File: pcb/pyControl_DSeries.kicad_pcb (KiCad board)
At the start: 2 copper layers, 90.2 x 66.5 mm, 14 parts, among them J1 Barrel_Jack, J2 RJ45-12PORT, U1 PyBoard-D-Series, U2 MC7805_DPAK, U3 TBD62083APG, U4 TBD62083APG, U5 TBD62083APG

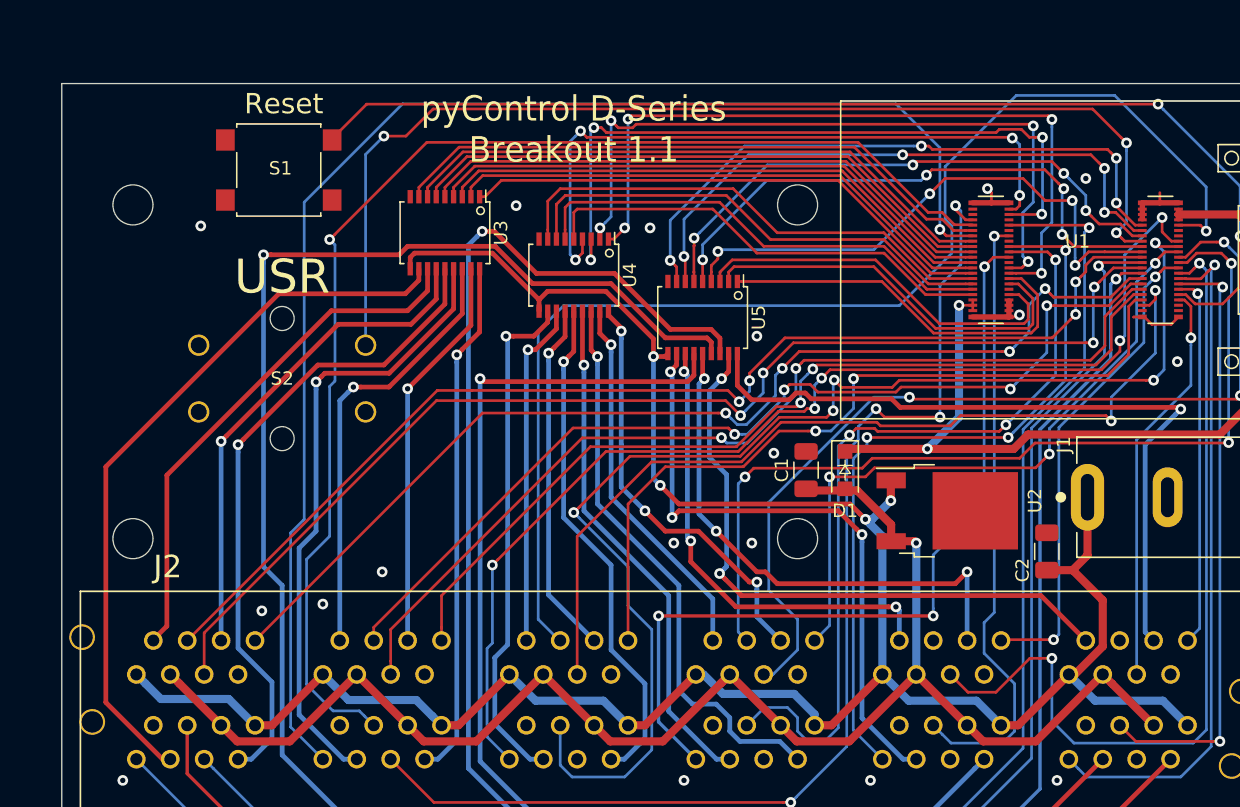
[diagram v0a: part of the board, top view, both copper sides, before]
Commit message: Revised PCB to v1.2 Switched from linear regulator to DC-DC converter. 1µF capacitors are now 10µF. Added TAPR link to silkscreen and schematic.
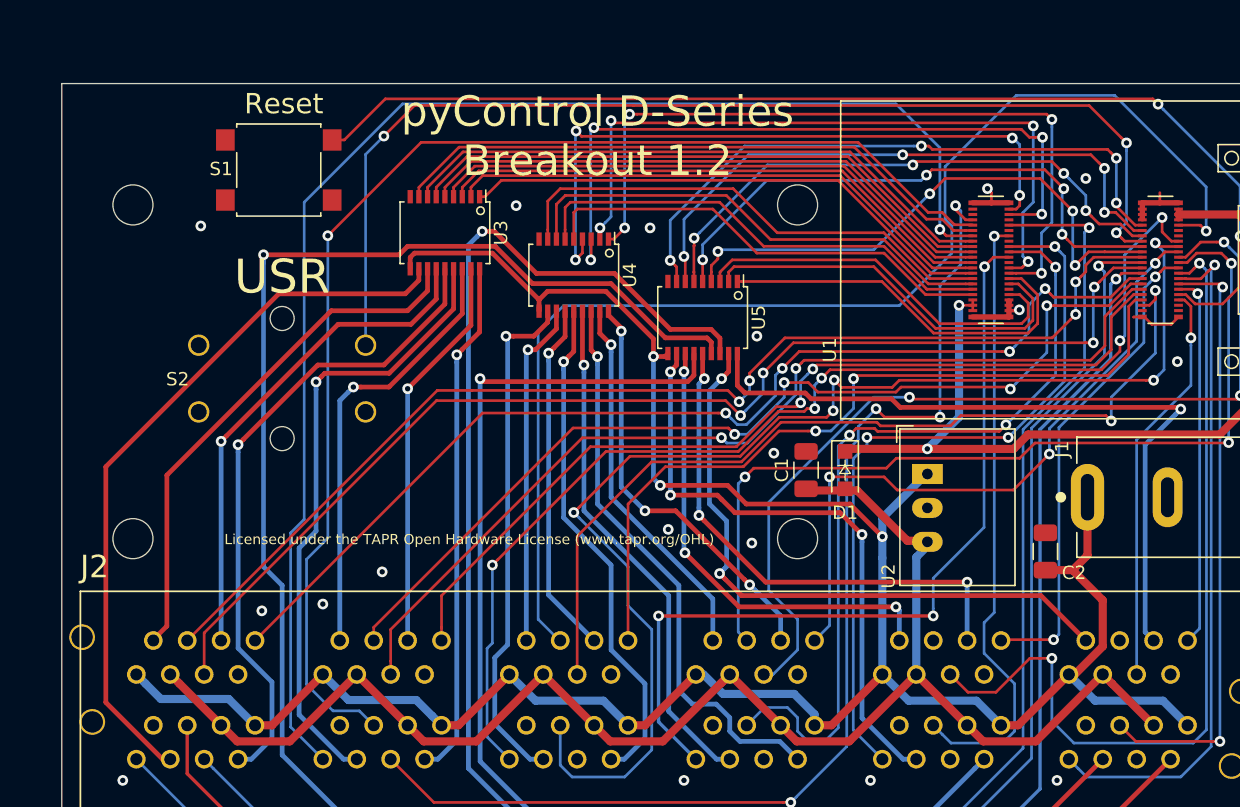
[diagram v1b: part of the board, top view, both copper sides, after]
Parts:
- C1, C2: value 1µF -> 10µF
- D1: footprint Andy_footprints:D_SOD-123F -> asl_footprints:D_SOD-123F
- DRA1, DRA2: footprint Andy_footprints:DIN_Clip -> asl_footprints:DIN_Clip
- J1: footprint Andy_footprints:DC_Jack -> asl_footprints:DC_Jack
- J2: footprint Andy_footprints:RJ45_12Port -> asl_footprints:RJ45_12Port
- S1: footprint Andy_footprints:6mm_tactile_smd -> asl_footprints:6mm_tactile_smd
- S2: footprint Andy_footprints:12mm_tactile_SPST -> asl_footprints:12mm_tactile_SPST
- U1: footprint Andy_footprints:PyBoard_D-Series -> asl_footprints:PyBoard_D-Series
- U2: value MC7805_DPAK -> R-78E5.0-1.0; footprint Andy_footprints:TO-252-2 -> asl_footprints:Converter_DCDC_RECOM_R-78E-0.5_THT
- U3, U4, U5: footprint Andy_footprints:SSOP-18_4.4x6.5mm_P0.65mm -> asl_footprints:SSOP-18_4.4x6.5mm_P0.65mm
- moved U2 3.13 mm to (116.9, 115.1), turned to 270 degrees
- moved C2 0.11 mm to (125.8, 120.9)
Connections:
- J2 pad B3-5: Net-(J2-PadB3-5) -> (no net)
- J2 pad B4-5: Net-(J2-PadB4-5) -> (no net)
- J2 pad B5-5: Net-(J2-PadB5-5) -> (no net)
- J2 pad B6-5: Net-(J2-PadB6-5) -> (no net)
- J2 pad S1: Net-(J2-PadS1) -> (no net)
- J2 pad S2: Net-(J2-PadS2) -> (no net)
- J2 pad S3: Net-(J2-PadS3) -> (no net)
- J2 pad S4: Net-(J2-PadS4) -> (no net)
- J2 pad S5: Net-(J2-PadS5) -> (no net)
- J2 pad S6: Net-(J2-PadS6) -> (no net)
- J2 pad T5-5: Net-(J2-PadT5-5) -> (no net)
- J2 pad T6-5: Net-(J2-PadT6-5) -> (no net)
- S1 pad 4: Net-(S1-Pad4) -> (no net)
- S2 pad 1: Net-(S2-Pad1) -> (no net)
- S2 pad 4: Net-(S2-Pad4) -> (no net)
- U1 pad 13: Net-(U1-Pad13) -> (no net)
- U1 pad 2: Net-(U1-Pad2) -> (no net)
- U1 pad 21: Net-(U1-Pad21) -> (no net)
- U1 pad 31: Net-(U1-Pad31) -> (no net)
- U1 pad 4: Net-(U1-Pad4) -> (no net)
- U1 pad 41: Net-(U1-Pad41) -> (no net)
- U1 pad 42: Net-(U1-Pad42) -> (no net)
- U1 pad 44: Net-(U1-Pad44) -> (no net)
- U1 pad 5: Net-(U1-Pad5) -> (no net)
- U1 pad 70: Net-(U1-Pad70) -> (no net)
- U1 pad 9: Net-(U1-Pad9) -> (no net)
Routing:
- net /12VDC: track 183.6 -> 186.2 mm, vias 4 -> 3
- net /B5_PA: track 46.8 -> 45.4 mm
- net /T5_PA: track 40.0 -> 38.9 mm
- net /5VDC: track 117.2 -> 118.3 mm, vias 1 -> 0
- net /T4_DA: track 49.6 -> 50.5 mm
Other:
- board text added: "Licensed under the TAPR Open Hardware License (www.tapr.org/OHL)"
- board text added: "pyControl D-Series Breakout 1.2"
- board text removed: "pyControl D-Series Breakout 1.1"

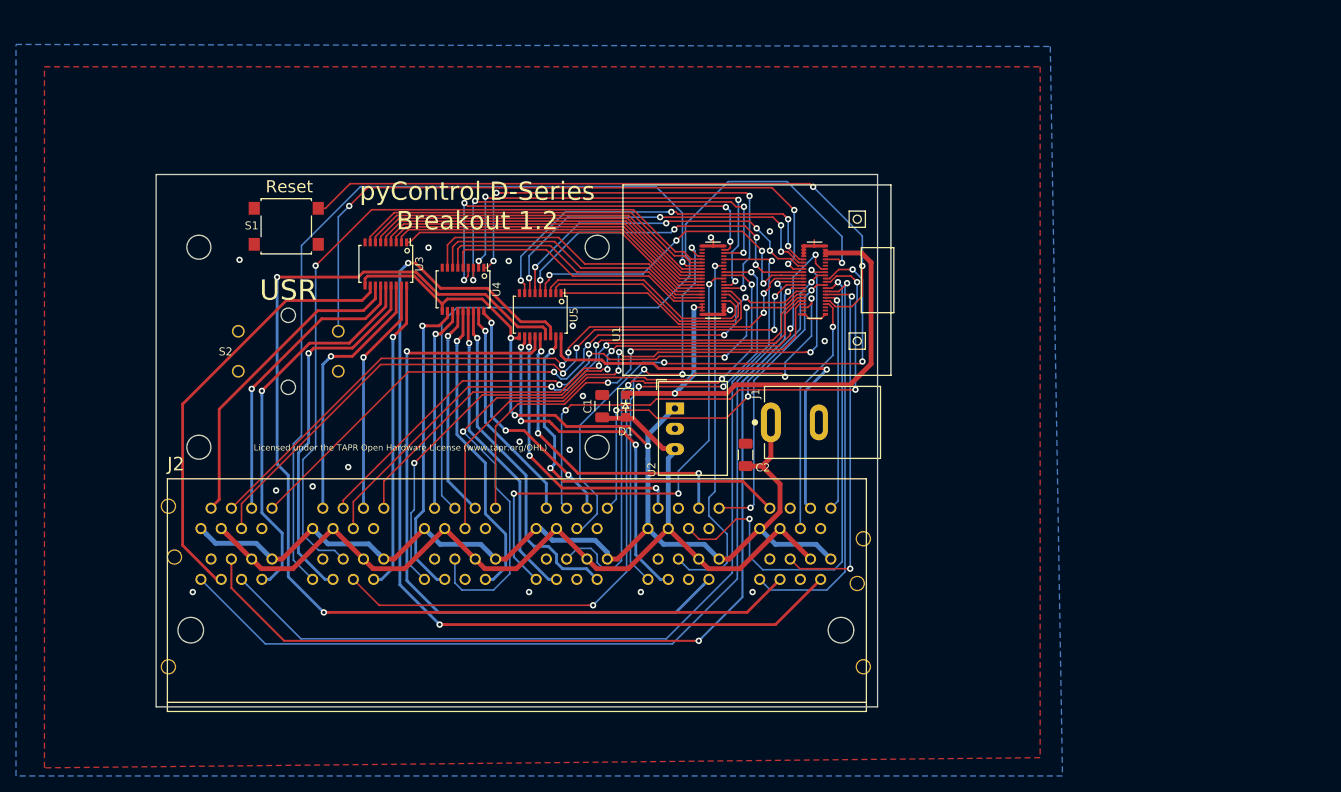
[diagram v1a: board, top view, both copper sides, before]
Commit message: pcb version 1.3. W1 cannot be used as DIO, so now B4_COMA is connected to pin9 (W9). W69 cannot be used as DIO, so now B5_COMB is connected to pin5 (W5). Added microusb connector so that you can permanently plug into breakout board and talk to the pyboard via the Hirose connector. This enables usb communication with the pyboard while still allowing one to easily swap out pyboards if necessary. changed user switch to SMD part Shifted components around.
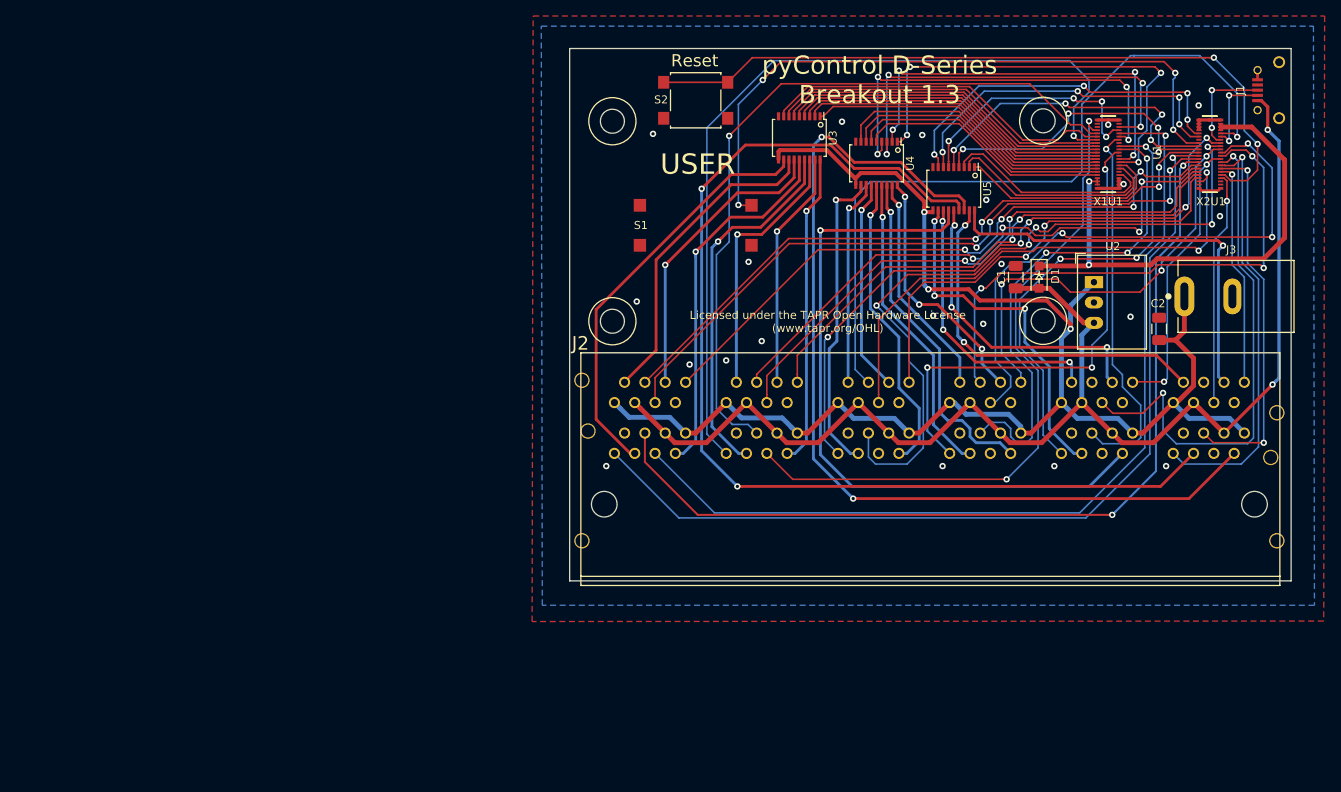
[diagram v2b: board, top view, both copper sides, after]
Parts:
- added J1: USB_micro_horz_socket_reinforced, asl_footprints:microUSB_horizontal_socket, F.Cu at (191.2, 75.3)
- added X1U1: Hirose_40_pin_connector, asl_footprints:Hirose_40_pin, F.Cu at (171.1, 83.3)
- added X2U1: Hirose_40_pin_connector, asl_footprints:Hirose_40_pin, F.Cu at (183.8, 83.3)
- S1: value B3FS-1010P -> TL3300; footprint asl_footprints:6mm_tactile_smd -> asl_footprints:12mm_tactile_smd
- S2: value B3F-4000 -> B3FS-1010P; footprint asl_footprints:12mm_tactile_SPST -> asl_footprints:6mm_tactile_smd
- moved S2 59.8 mm to (119.5, 76.6)
- moved DRA2 57.9 mm to (162.9, 91.6)
- moved U2 54.7 mm to (169.3, 99.3)
- moved C1 54.1 mm to (159.5, 98.7)
- moved D1 54.1 mm to (162.4, 98.7)
- moved J2 54.0 mm to (148.8, 122.7)
- moved J3 54.0 mm to (180.6, 101.1)
- moved U3 54.0 mm to (132.5, 81.3)
- moved U4 54.0 mm to (142.1, 84.5)
- moved U5 54.0 mm to (151.8, 87.6)
- moved DRA1 54.0 mm to (109.1, 91.7)
- moved C2 54.0 mm to (177.4, 105.2)
- moved U1 51.9 mm to (177.4, 83.3)
- moved S1 51.2 mm to (119.5, 92.2)
- renumbered J1 to J3
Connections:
- S1 pad 3: /RST -> /USR
- S2 pad 1: (no net) -> /GND
- S2 pad 3: /USR -> /RST
- S2 pad 4: (no net) -> /RST
- U1 pad 1: /B4_COMA -> (no net)
- U1 pad 5: (no net) -> /B5_COMB
- U1 pad 69: /B5_COMB -> (no net)
- U1 pad 70: (no net) -> Net-(J1-PadP3)
- U1 pad 72: (no net) -> Net-(J1-PadP2)
- U1 pad 9: (no net) -> /B4_COMA
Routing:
- net /5VDC: track 118.3 -> 165.0 mm, vias 0 -> 2
- net Net-(J1-PadP3): track 0.00 -> 12.7 mm, vias 0 -> 2
- net /B5_COMB: track 42.2 -> 31.4 mm
- net Net-(J1-PadP2): track 0.00 -> 10.6 mm, vias 0 -> 2
- net /RST: track 84.9 -> 91.5 mm
- net /B6_PA: track 140.7 -> 136.1 mm
- net /B3_DA: track 84.0 -> 79.5 mm
- net /T4_DA: track 50.5 -> 54.0 mm
- net /B6_COMA: track 41.9 -> 38.4 mm
- net /B3_DB: track 93.3 -> 90.1 mm
- net /T6_PA: track 55.0 -> 51.9 mm
- net /T1_DB: track 88.9 -> 85.9 mm
- net /B3_COMB: track 34.6 -> 31.7 mm
- net /T1_DC: track 86.7 -> 83.7 mm
- net /T3_COMA: track 35.8 -> 32.9 mm
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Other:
- board text added: "USER"
- board text added: "pyControl D-Series Breakout 1.3"
- board text removed: "USR"
- board text removed: "pyControl D-Series Breakout 1.2"

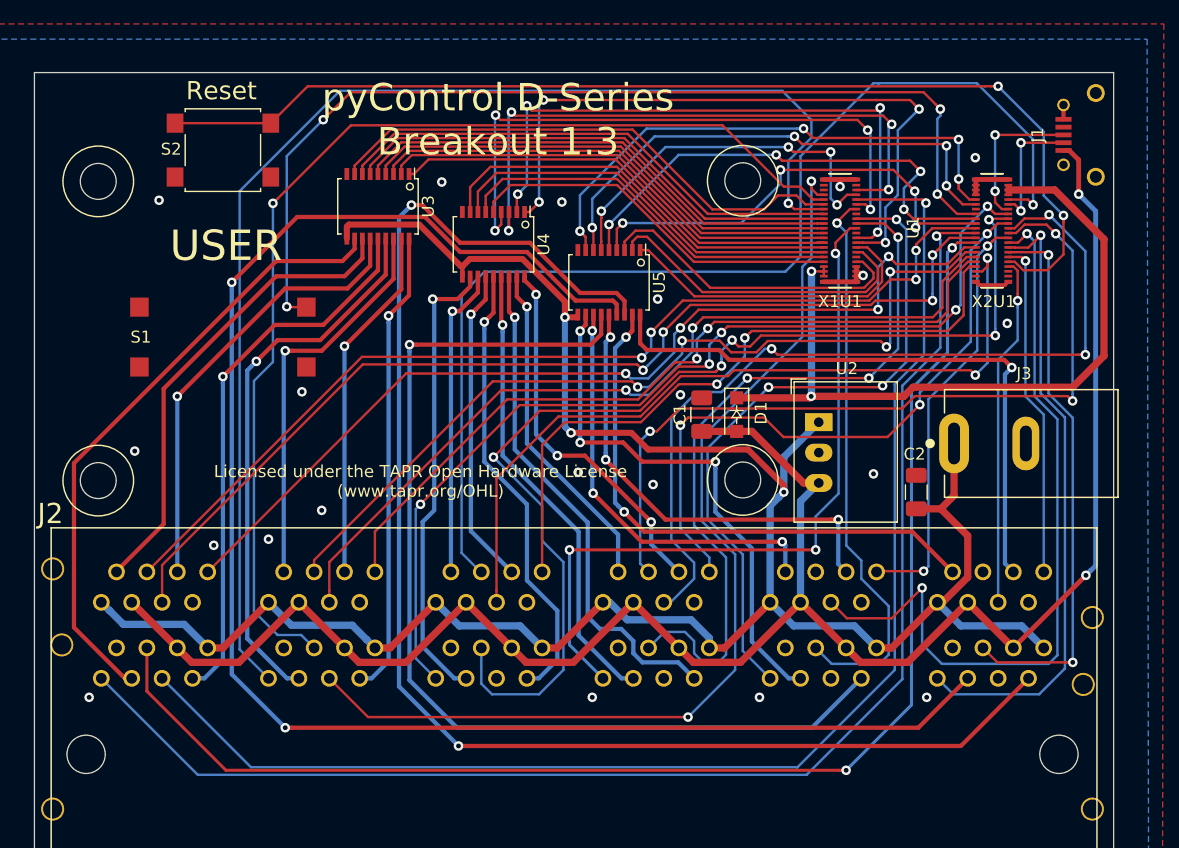
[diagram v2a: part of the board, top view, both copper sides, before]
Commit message: PCB rev 1.4 removed mounting pads from D40 Hirose connector since that version of connector is discontinued. shifted pyboard connectors down and to the left so now an SD card can be inserted without interfering with microusb connector micro usb tx/rx were incorrectly wired. swapped buttons so user button is now closer to board edge (less likely to accidentally press reset on way to pressing user button).
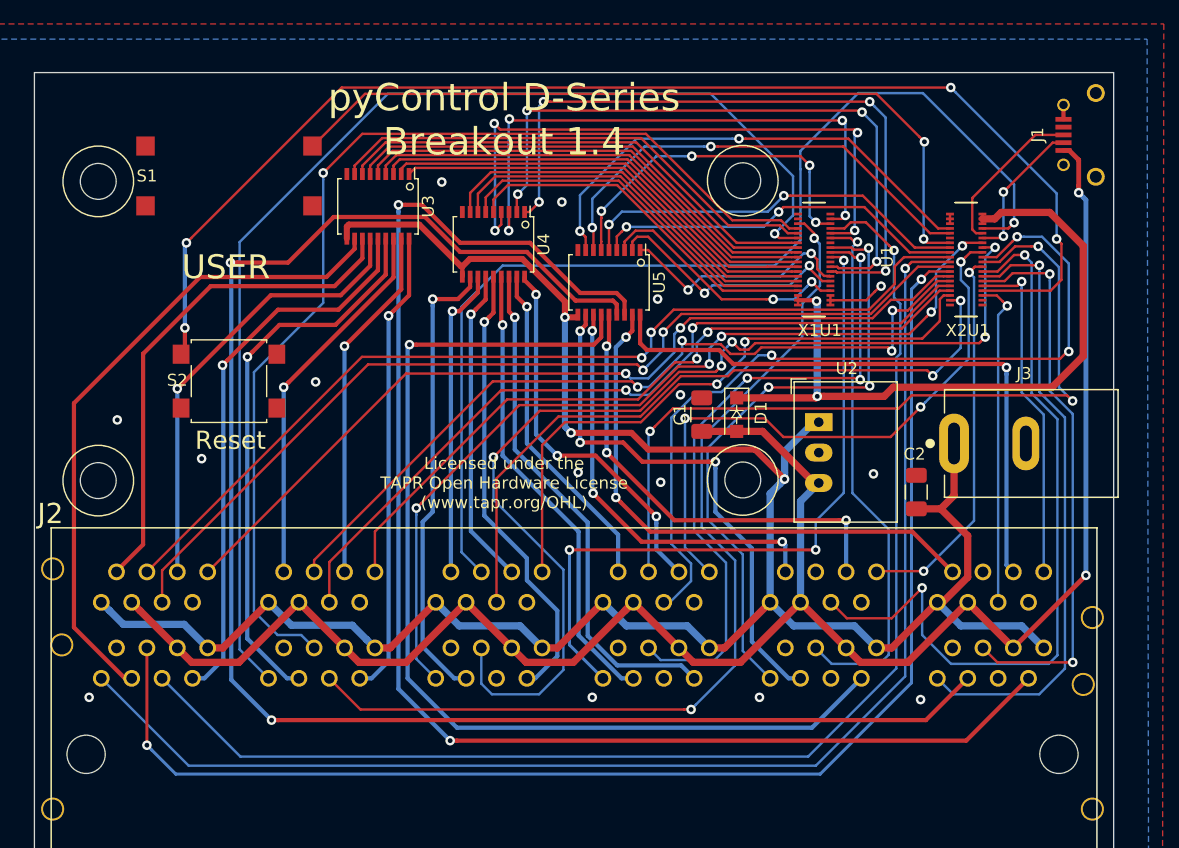
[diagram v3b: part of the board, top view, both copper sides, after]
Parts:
- moved S2 19.3 mm to (120.0, 95.9)
- moved S1 13.5 mm to (120.0, 78.7)
- moved U1 3.24 mm to (175.3, 85.7)
- moved X1U1 3.24 mm to (168.9, 85.7)
- moved X2U1 3.24 mm to (181.6, 85.7)
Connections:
- S2 pad 3: /RST -> (no net)
- U1 pad 70: Net-(J1-PadP3) -> Net-(J1-PadP2)
- U1 pad 72: Net-(J1-PadP2) -> Net-(J1-PadP3)
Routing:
- net /USR: track 82.8 -> 65.1 mm, vias 4 -> 2
- net /RST: track 91.5 -> 105.6 mm, vias 2 -> 4
- net /GND: track 17.1 -> 8.49 mm, vias 21 -> 15
- net /T5_COMA: track 41.2 -> 33.4 mm, vias 4 -> 2
- net /T3_DB: track 66.3 -> 58.9 mm
- net /T6_COMA: track 26.6 -> 19.8 mm, vias 0 -> 2
- net /B6_COMA: track 38.4 -> 31.6 mm, vias 4 -> 2
- net /B4_DB: track 61.9 -> 55.3 mm
- net /T6_COMB: track 27.1 -> 21.0 mm, vias 0 -> 2
- net /T1_DA: track 79.2 -> 73.5 mm, vias 4 -> 2
- net /B3_DA: track 79.5 -> 73.8 mm
- net /B2_DA: track 104.9 -> 99.2 mm
- net /T1_DB: track 85.9 -> 80.3 mm, vias 4 -> 2
- net /B6_COMB: track 26.5 -> 21.6 mm, vias 0 -> 2
- net /B1_DAC: track 113.7 -> 108.9 mm
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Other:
- board text added: "pyControl D-Series Breakout 1.4"
- board text removed: "pyControl D-Series Breakout 1.3"
